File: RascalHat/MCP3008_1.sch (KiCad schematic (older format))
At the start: 5 parts, among them U2 MCP3008, U3 MCP3008

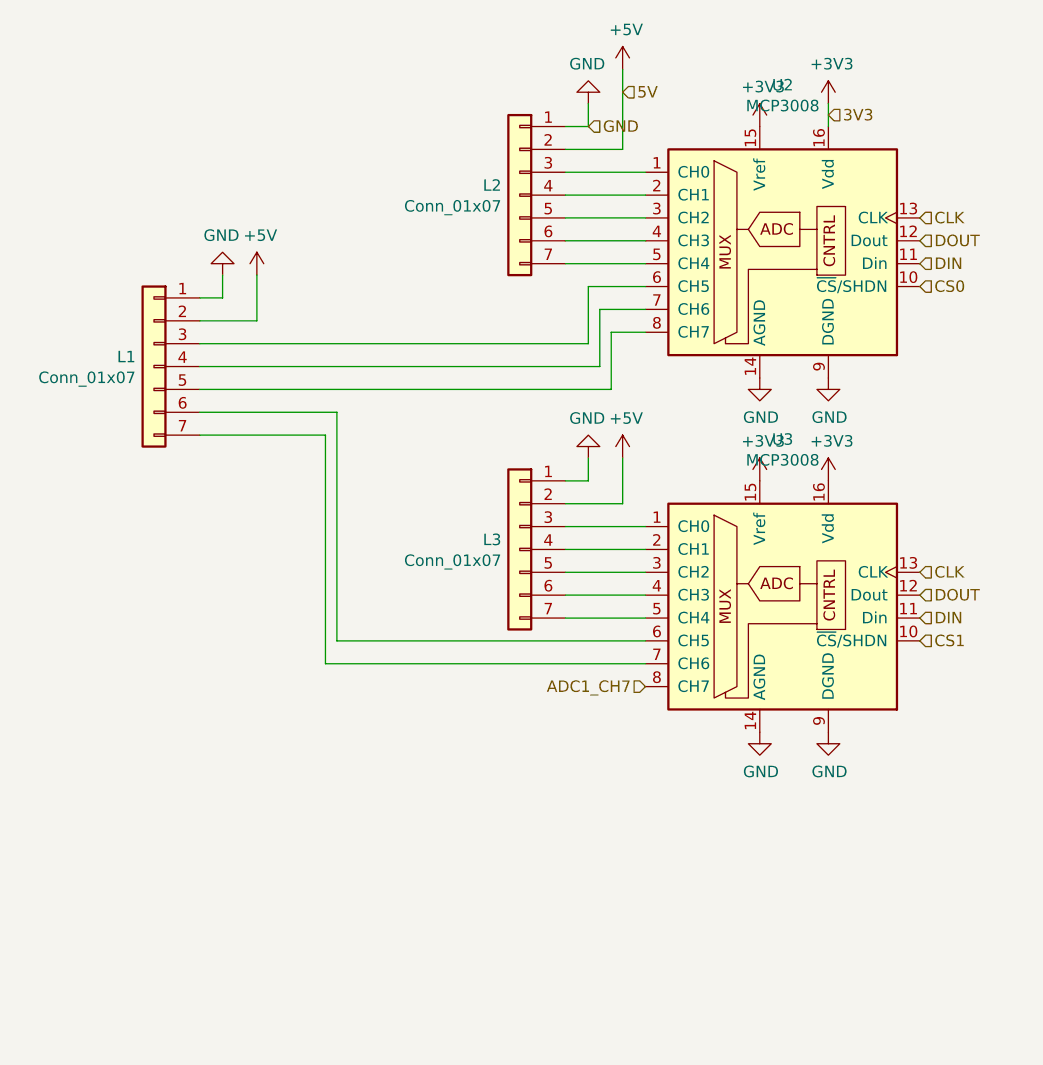
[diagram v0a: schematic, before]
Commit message: schematic done, symbol-footprint done, pcb started
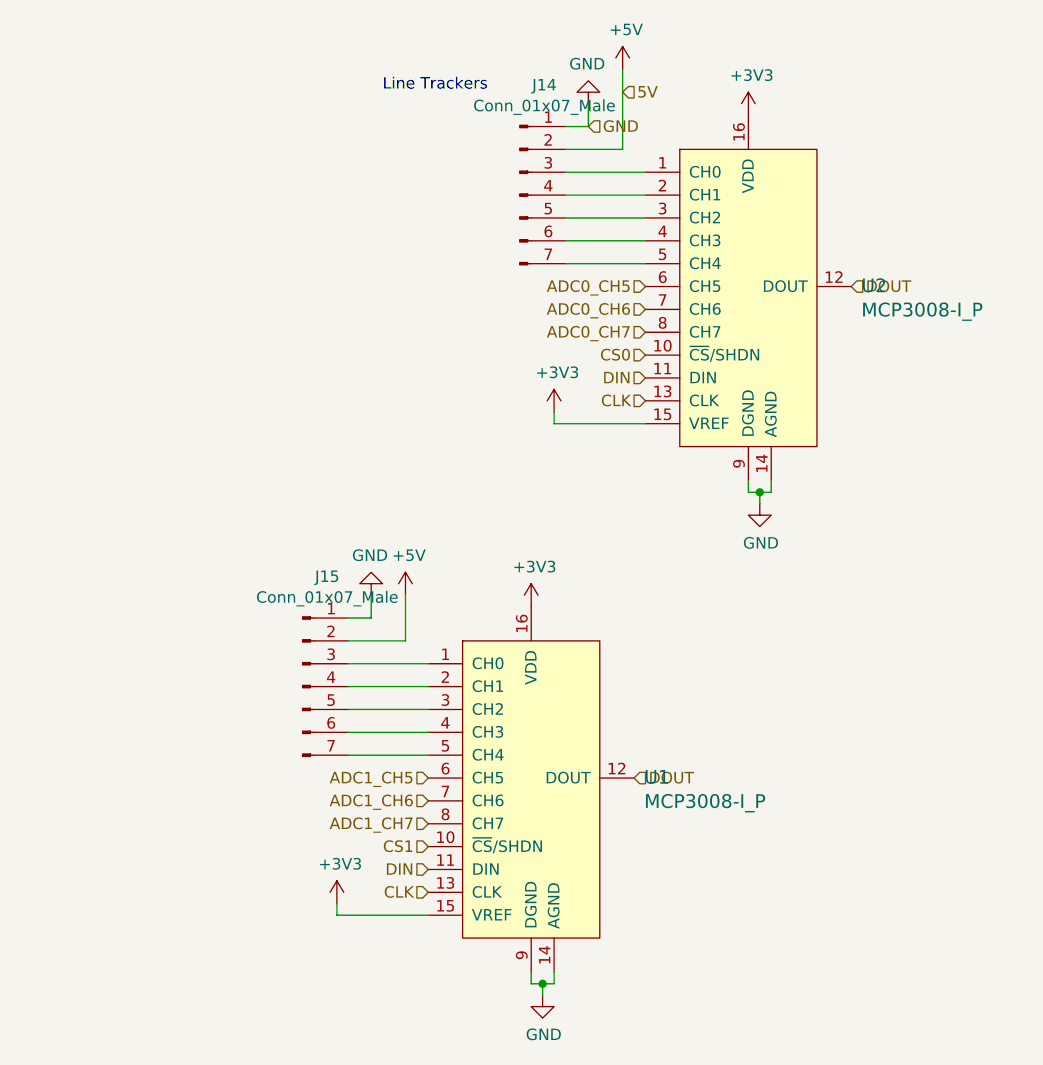
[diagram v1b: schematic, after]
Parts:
- removed L1, L2, L3: Conn_01x07, symbol Connector_Generic:Conn_01x07
- removed U2, U3: MCP3008, symbol Analog_ADC:MCP3008
- added J14, J15: Conn_01x07_Male, Connector_JST:JST_EH_B7B-EH-A_1x07_P2.50mm_Vertical, symbol Connector:Conn_01x07_Male
- added U1, U2: MCP3008-I_P, digikey-footprints:DIP-16_W7.62mm, symbol dk_Data-Acquisition-Analog-to-Digital-Converters-ADC:MCP3008-I_P
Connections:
- net +3V3: now also U1.15 (VREF), U1.16 (VDD), U2.15 (VREF), U2.16 (VDD)
- net +5V: now also J14.2 (Pin_2), J15.2 (Pin_2)
- net ADC1_CH7: now also U1.8 (CH7)
- net CLK: now also U1.13 (CLK), U2.13 (CLK)
- net CS0: now also U2.10 (~CS~/SHDN)
- net CS1: now also U1.10 (~CS~/SHDN)
- net DIN: now also U1.11 (DIN), U2.11 (DIN)
- net DOUT: now also U1.12 (DOUT), U2.12 (DOUT)
- net GND: now also J14.1 (Pin_1), J15.1 (Pin_1), U1.14 (AGND), U1.9 (DGND), U2.14 (AGND), U2.9 (DGND)
- new net: J14.3 (Pin_3), U2.1 (CH0)
- new net: J14.4 (Pin_4), U2.2 (CH1)
- new net: J14.5 (Pin_5), U2.3 (CH2)
- new net: J14.6 (Pin_6), U2.4 (CH3)
- new net: J14.7 (Pin_7), U2.5 (CH4)
- new net: J15.3 (Pin_3), U1.1 (CH0)
- new net: J15.4 (Pin_4), U1.2 (CH1)
- new net: J15.5 (Pin_5), U1.3 (CH2)
- new net: J15.6 (Pin_6), U1.4 (CH3)
- new net: J15.7 (Pin_7), U1.5 (CH4)
- new net ADC0_CH5: U2.6 (CH5)
- new net ADC0_CH6: U2.7 (CH6)
- new net ADC0_CH7: U2.8 (CH7)
- new net ADC1_CH5: U1.6 (CH5)
- new net ADC1_CH6: U1.7 (CH6)
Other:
- note added: "Line Trackers"

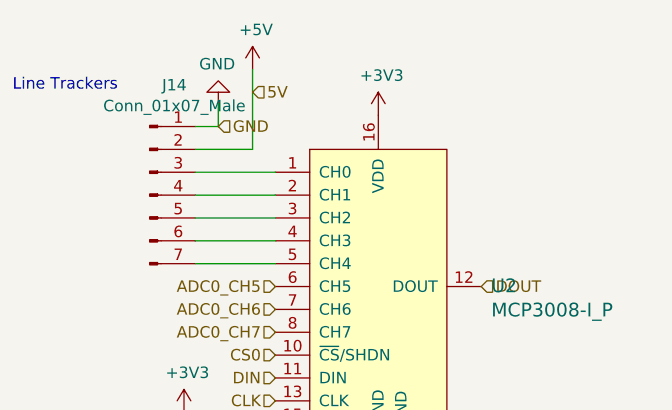
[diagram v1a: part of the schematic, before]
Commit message: schematic updated, all footprints created, pcb layout started
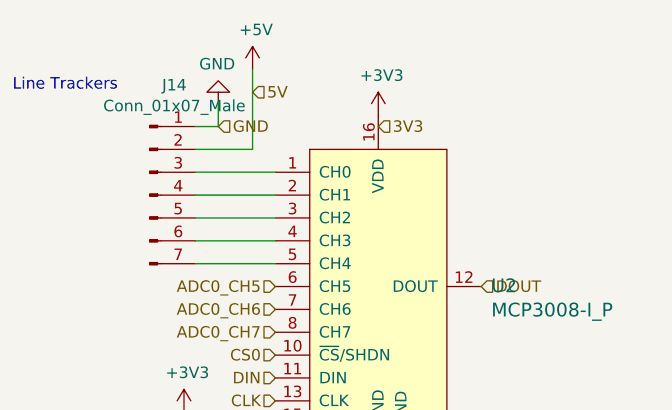
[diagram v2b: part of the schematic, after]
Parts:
- U1, U2: footprint digikey-footprints:DIP-16_W7.62mm -> Package_SO:SOIC-16_3.9x9.9mm_P1.27mm
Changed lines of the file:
@@
 F 0 "U2" H 7444 3703 60  0000 L CNN
 F 1 "MCP3008-I_P" H 7444 3597 60  0000 L CNN
-F 2 "digikey-footprints:DIP-16_W7.62mm" H 7150 3900 60  0001 L CNN
+F 2 "Package_SO:SOIC-16_3.9x9.9mm_P1.27mm" H 7150 3900 60  0001 L CNN
 F 3 "http://www.microchip.com/mymicrochip/filehandler.aspx?ddocname=en011593" H 7150 4000 60  0001 L CNN
 F 4 "MCP3008-I/P-ND" H 7150 4100 60  0001 L CNN "Digi-Key_PN"
@@
 F 0 "U1" H 6494 5853 60  0000 L CNN
 F 1 "MCP3008-I_P" H 6494 5747 60  0000 L CNN
-F 2 "digikey-footprints:DIP-16_W7.62mm" H 6200 6050 60  0001 L CNN
+F 2 "Package_SO:SOIC-16_3.9x9.9mm_P1.27mm" H 6200 6050 60  0001 L CNN
 F 3 "http://www.microchip.com/mymicrochip/filehandler.aspx?ddocname=en011593" H 6200 6150 60  0001 L CNN
 F 4 "MCP3008-I/P-ND" H 6200 6250 60  0001 L CNN "Digi-Key_PN"
@@
 Wire Wire Line
 	5150 6450 5550 6450
+Text HLabel 6950 3000 2    50   Input ~ 0
+3V3
 $EndSCHEMATC
